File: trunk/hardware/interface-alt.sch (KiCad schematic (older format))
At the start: 19 parts, among them SW1 DIPSW4_DIP, U4 GTL2003

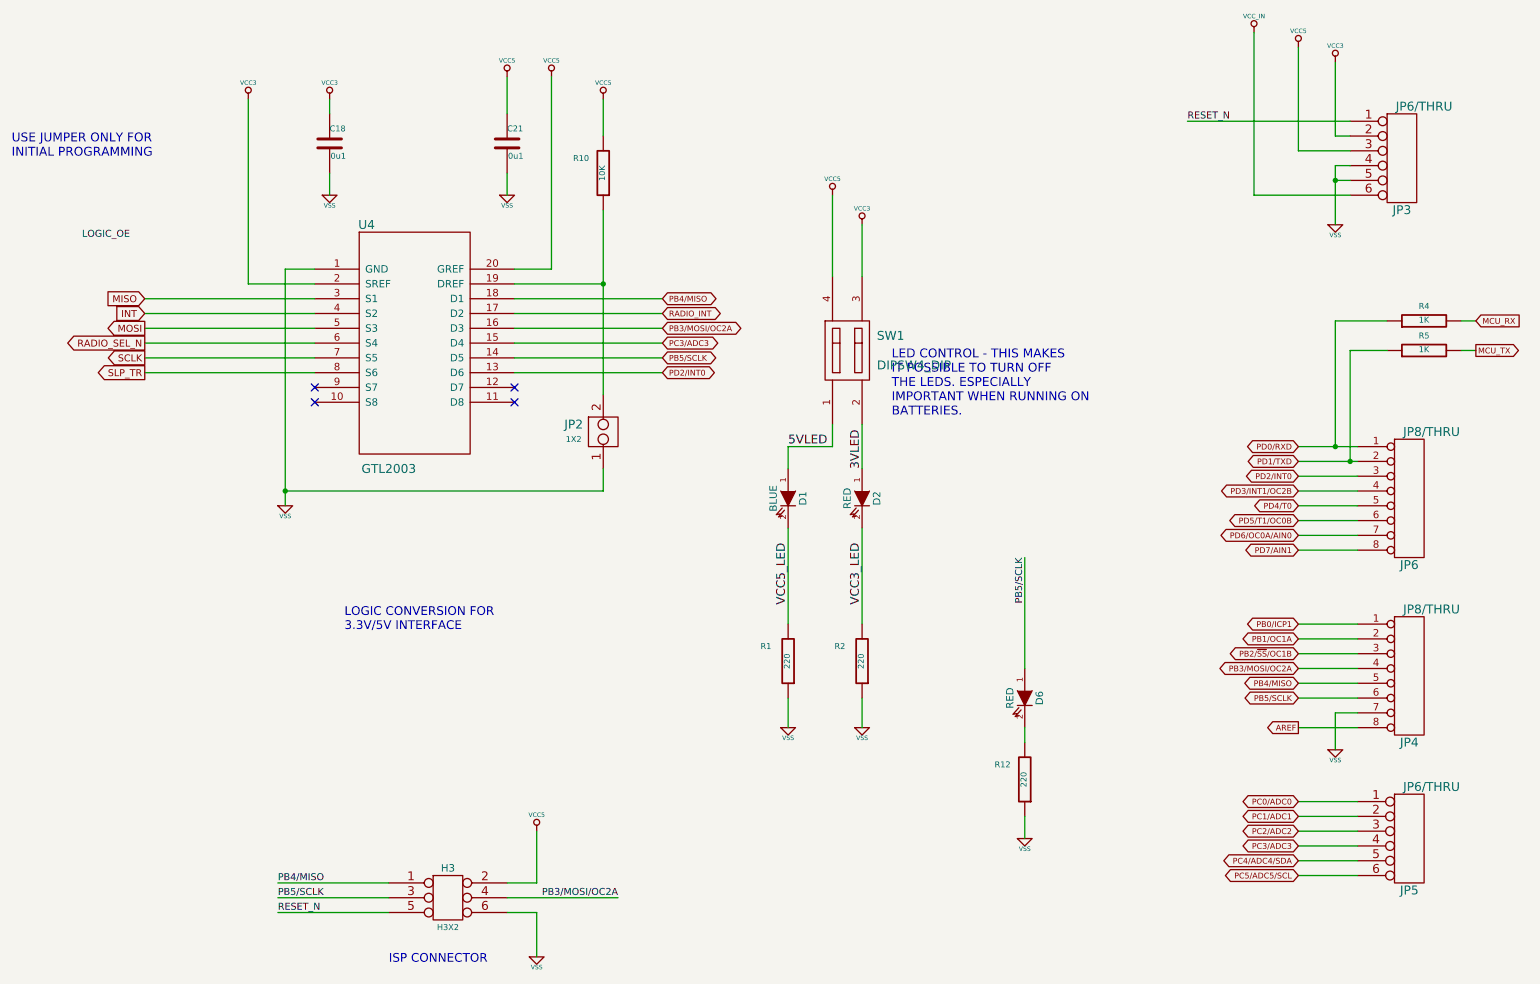
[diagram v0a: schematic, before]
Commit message: SCH: minor corrections to interface-alt.sch
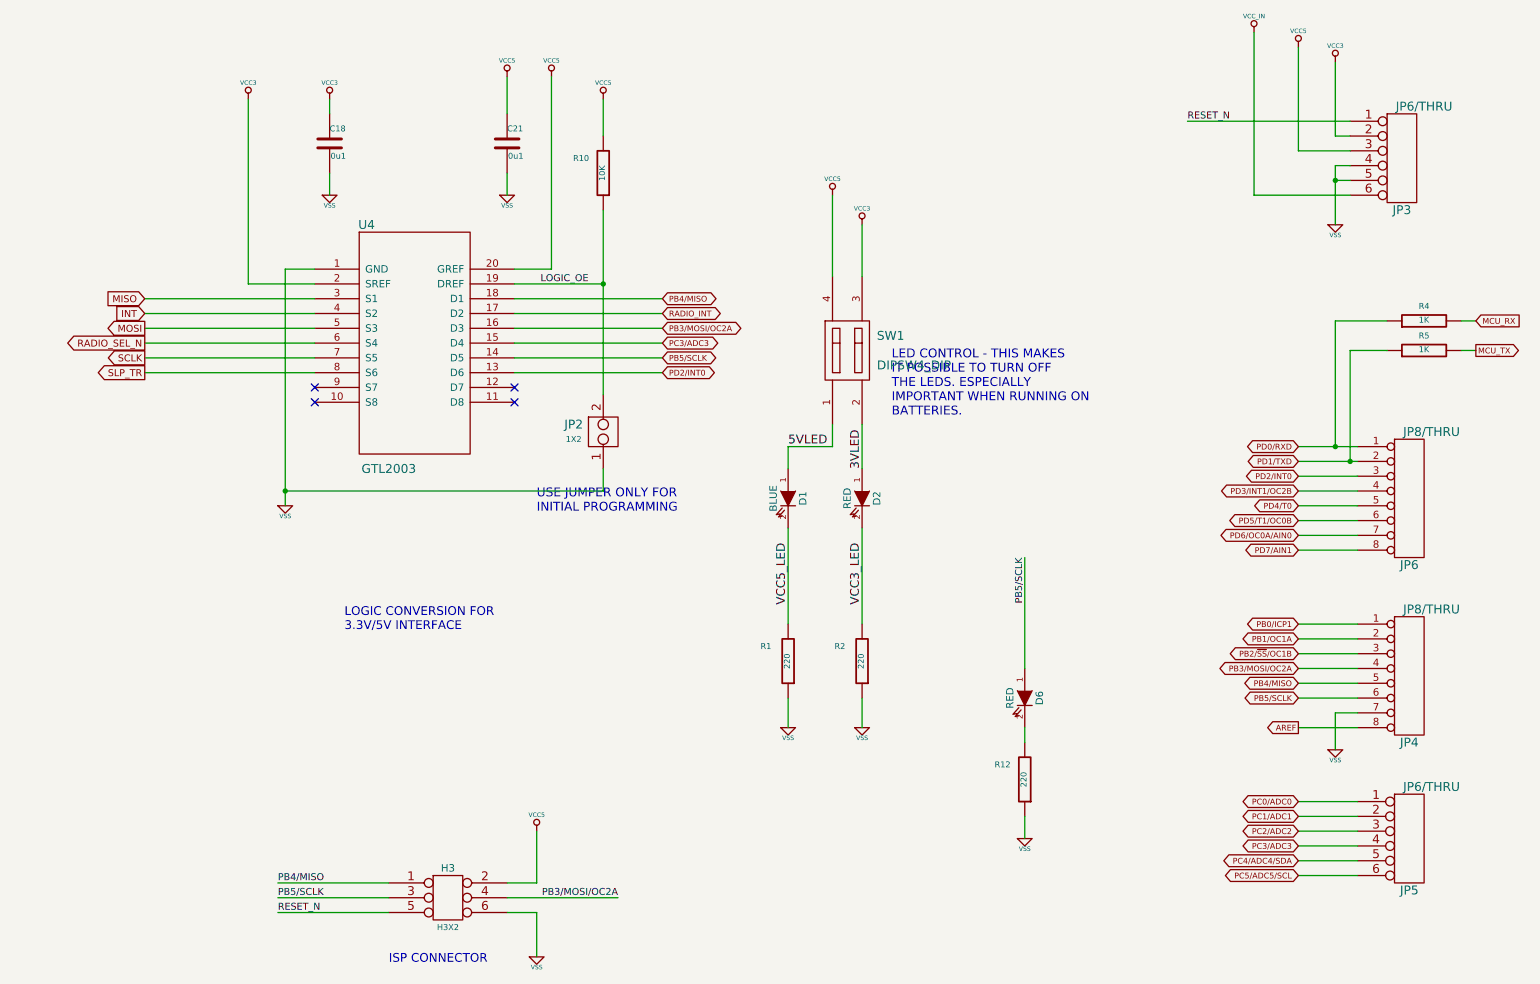
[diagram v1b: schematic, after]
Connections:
- net LOGIC_OE: now also JP2.2, R10.1, U4.19 (DREF)
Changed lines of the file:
@@
 Sheet 2 6
 Title "FREAKDUINO-CHIBI 2.4GHz"
-Date "16 jul 2013"
+Date "17 jul 2013"
 Rev "v2.1a"
 Comp "KiCAD version by Gruvin"
@@
 NoConn ~ 4100 3400
 Wire Wire Line
-	4700 2200 4700 2700
-Wire Wire Line
-	4700 2700 4700 3450
+	4700 2200 4700 3450
 $Comp
 L VSS #PWR012
@@
 Wire Wire Line
 	2750 3300 1600 3300
-Text Label 1500 2400 2    47   ~ 0
+Text Label 4600 2700 2    47   ~ 0
 LOGIC_OE
 Text GLabel 1600 2800 0    47   Input ~ 0
@@
 	1    0    0    -1
 $EndComp
-Text Notes 700  1850 0    60   ~ 0
+Text Notes 4250 4250 0    60   ~ 0
 USE JUMPER ONLY FOR\nINITIAL PROGRAMMING
 $Comp
@@
 	5950 4350 5950 5000
 $Comp
-L VSS #PWR019
+L VSS #PWR018
 U 1 1 51E3E179
 P 5950 5700
-F 0 "#PWR019" H 5950 5700 30  0001 C CNN
+F 0 "#PWR018" H 5950 5700 30  0001 C CNN
 F 1 "VSS" H 5950 5630 30  0000 C CNN
 F 2 "" H 5950 5700 60  0000 C CNN
@@
 $EndComp
 $Comp
-L VSS #PWR020
+L VSS #PWR019
 U 1 1 51E3E17F
 P 6450 5700
-F 0 "#PWR020" H 6450 5700 30  0001 C CNN
+F 0 "#PWR019" H 6450 5700 30  0001 C CNN
 F 1 "VSS" H 6450 5630 30  0000 C CNN
 F 2 "" H 6450 5700 60  0000 C CNN
@@
 VCC3_LED
 $Comp
-L VCC3 #PWR021
+L VCC3 #PWR020
 U 1 1 51E3E18C
 P 6450 2300
-F 0 "#PWR021" H 6450 2440 20  0001 C CNN
+F 0 "#PWR020" H 6450 2440 20  0001 C CNN
 F 1 "VCC3" H 6450 2410 30  0000 C CNN
 F 2 "" H 6450 2300 60  0000 C CNN
@@
 $EndComp
 $Comp
-L VCC5 #PWR022
+L VCC5 #PWR021
 U 1 1 51E3E192
 P 6250 2100
-F 0 "#PWR022" H 6250 2240 20  0001 C CNN
+F 0 "#PWR021" H 6250 2240 20  0001 C CNN
 F 1 "VCC5" H 6250 2210 30  0000 C CNN
 F 2 "" H 6250 2100 60  0000 C CNN
@@
 	4250 6950 4250 7250
 $Comp
-L VSS #PWR023
+L VSS #PWR022
 U 1 1 51E3E429
 P 4250 7250
-F 0 "#PWR023" H 4250 7250 30  0001 C CNN
+F 0 "#PWR022" H 4250 7250 30  0001 C CNN
 F 1 "VSS" H 4250 7180 30  0000 C CNN
 F 2 "" H 4250 7250 60  0000 C CNN
@@
 ISP CONNECTOR
 $Comp
-L VCC5 #PWR024
+L VCC5 #PWR023
 U 1 1 51E3E434
 P 4250 6400
-F 0 "#PWR024" H 4250 6540 20  0001 C CNN
+F 0 "#PWR023" H 4250 6540 20  0001 C CNN
 F 1 "VCC5" H 4250 6510 30  0000 C CNN
 F 2 "" H 4250 6400 60  0000 C CNN
@@
 $EndComp
 $Comp
-L VSS #PWR025
+L VSS #PWR024
 U 1 1 51E3E736
 P 7550 6450
-F 0 "#PWR025" H 7550 6450 30  0001 C CNN
+F 0 "#PWR024" H 7550 6450 30  0001 C CNN
 F 1 "VSS" H 7550 6380 30  0000 C CNN
 F 2 "" H 7550 6450 60  0000 C CNN
@@
 PB5/SCLK
 Wire Wire Line
-	9400 3800 9650 3800
-Wire Wire Line
-	9650 3800 9800 3800
-Wire Wire Line
-	9400 3900 9750 3900
-Wire Wire Line
-	9750 3900 9800 3900
+	9400 3800 9800 3800
+Wire Wire Line
+	9400 3900 9800 3900
 Wire Wire Line
 	9800 4000 9400 4000
@@
 	9650 5600 9650 5850
 $Comp
-L VSS #PWR026
+L VSS #PWR025
 U 1 1 51E3E76E
 P 9650 5850
-F 0 "#PWR026" H 9650 5850 30  0001 C CNN
+F 0 "#PWR025" H 9650 5850 30  0001 C CNN
 F 1 "VSS" H 9650 5780 30  0000 C CNN
 F 2 "" H 9650 5850 60  0000 C CNN
@@
 	9100 2100 9100 1000
 $Comp
-L VSS #PWR027
+L VSS #PWR026
 U 1 1 51E3E798
 P 9650 2300
-F 0 "#PWR027" H 9650 2300 30  0001 C CNN
+F 0 "#PWR026" H 9650 2300 30  0001 C CNN
 F 1 "VSS" H 9650 2230 30  0000 C CNN
 F 2 "" H 9650 2300 60  0000 C CNN
@@
 	9750 1900 9650 1900
 Wire Wire Line
-	9650 1900 9650 2000
-Wire Wire Line
-	9650 2000 9650 2300
+	9650 1900 9650 2300
 Wire Wire Line
 	9750 2000 9650 2000
 Connection ~ 9650 2000
 $Comp
-L VCC5 #PWR028
+L VCC5 #PWR027
 U 1 1 51E3E7A3
 P 9400 1100
-F 0 "#PWR028" H 9400 1240 20  0001 C CNN
+F 0 "#PWR027" H 9400 1240 20  0001 C CNN
 F 1 "VCC5" H 9400 1210 30  0000 C CNN
 F 2 "" H 9400 1100 60  0000 C CNN
@@
 $EndComp
 $Comp
-L VCC3 #PWR029
+L VCC3 #PWR028
 U 1 1 51E3E7A9
 P 9650 1200
-F 0 "#PWR029" H 9650 1340 20  0001 C CNN
+F 0 "#PWR028" H 9650 1340 20  0001 C CNN
 F 1 "VCC3" H 9650 1310 30  0000 C CNN
 F 2 "" H 9650 1200 60  0000 C CNN
@@
 $EndComp
 $Comp
-L VCC_IN #PWR030
+L VCC_IN #PWR029
 U 1 1 51E3E7C7
 P 9100 1000
-F 0 "#PWR030" H 9100 1140 20  0001 C CNN
+F 0 "#PWR029" H 9100 1140 20  0001 C CNN
 F 1 "VCC_IN" H 9100 1110 30  0000 C CNN
 F 2 "" H 9100 1000 60  0000 C CNN
@@
 	2750 2600 2550 2600
 Wire Wire Line
-	2550 2600 2550 4100
-Wire Wire Line
-	2550 4100 2550 4200
+	2550 2600 2550 4200
 Wire Wire Line
 	4700 3950 4700 4100
@@
 	2300 2700 2750 2700
 $Comp
-L VCC5 #PWR?
+L VCC5 #PWR030
 U 1 1 51E5EC37
 P 4700 1450
-F 0 "#PWR?" H 4700 1590 20  0001 C CNN
+F 0 "#PWR030" H 4700 1590 20  0001 C CNN
 F 1 "VCC5" H 4700 1560 30  0000 C CNN
 F 2 "" H 4700 1450 60  0000 C CNN
